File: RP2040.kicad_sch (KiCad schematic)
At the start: 30 parts, among them J1 USB_B_Micro, J2 Conn_01x03, SW1 SW_Push, SW2 SW_Push, U1 AMS1117-3.3, U5 W25Q128JVS, U6 RP2040, Y1 X322512MSB4SI

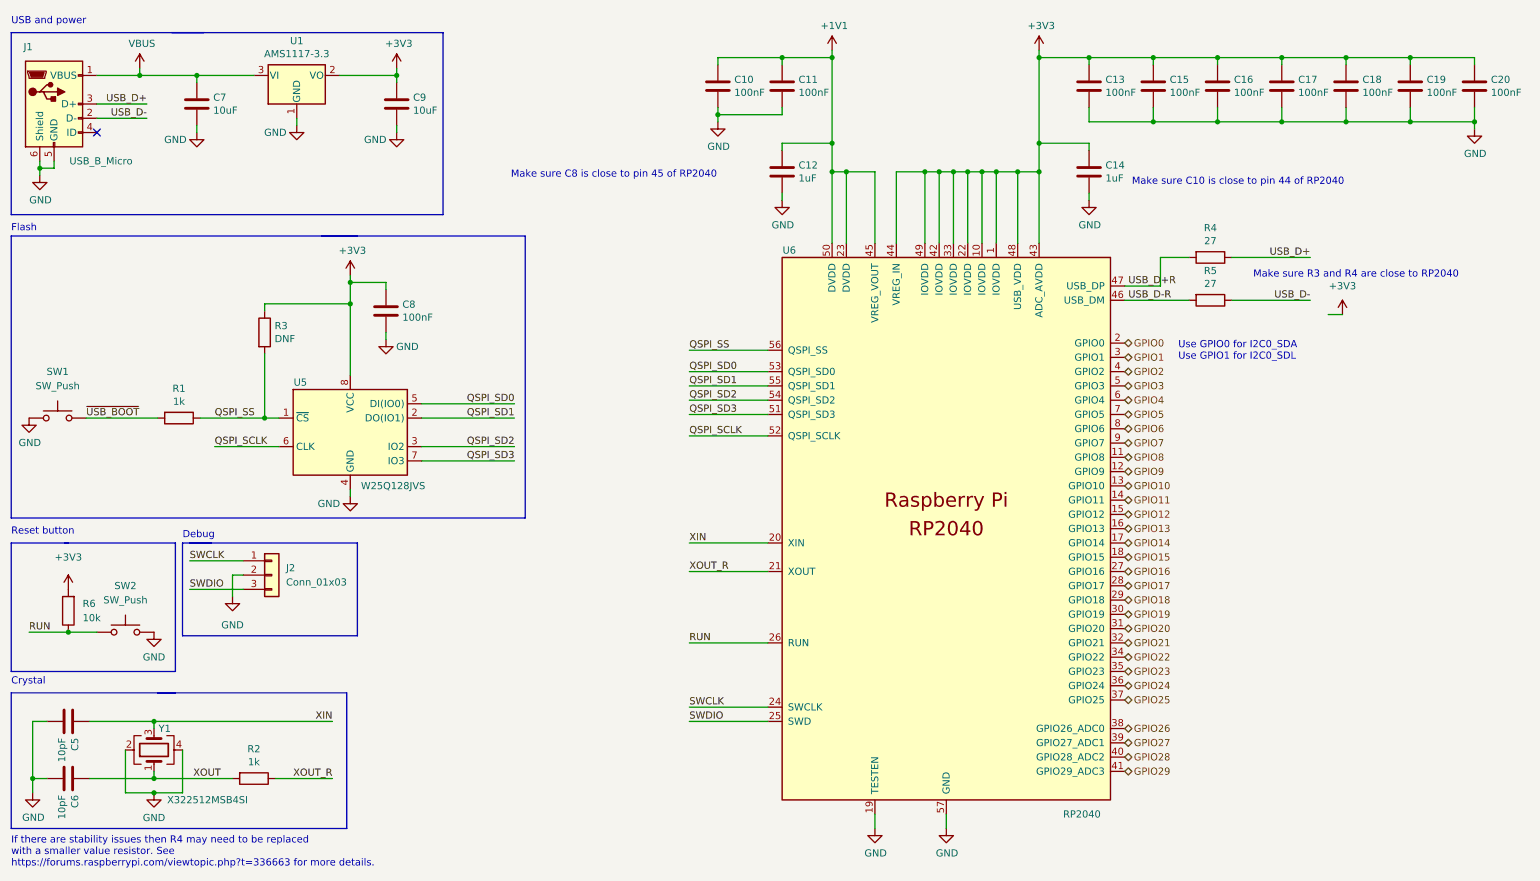
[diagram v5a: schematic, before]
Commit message: Redo RP2040 layout
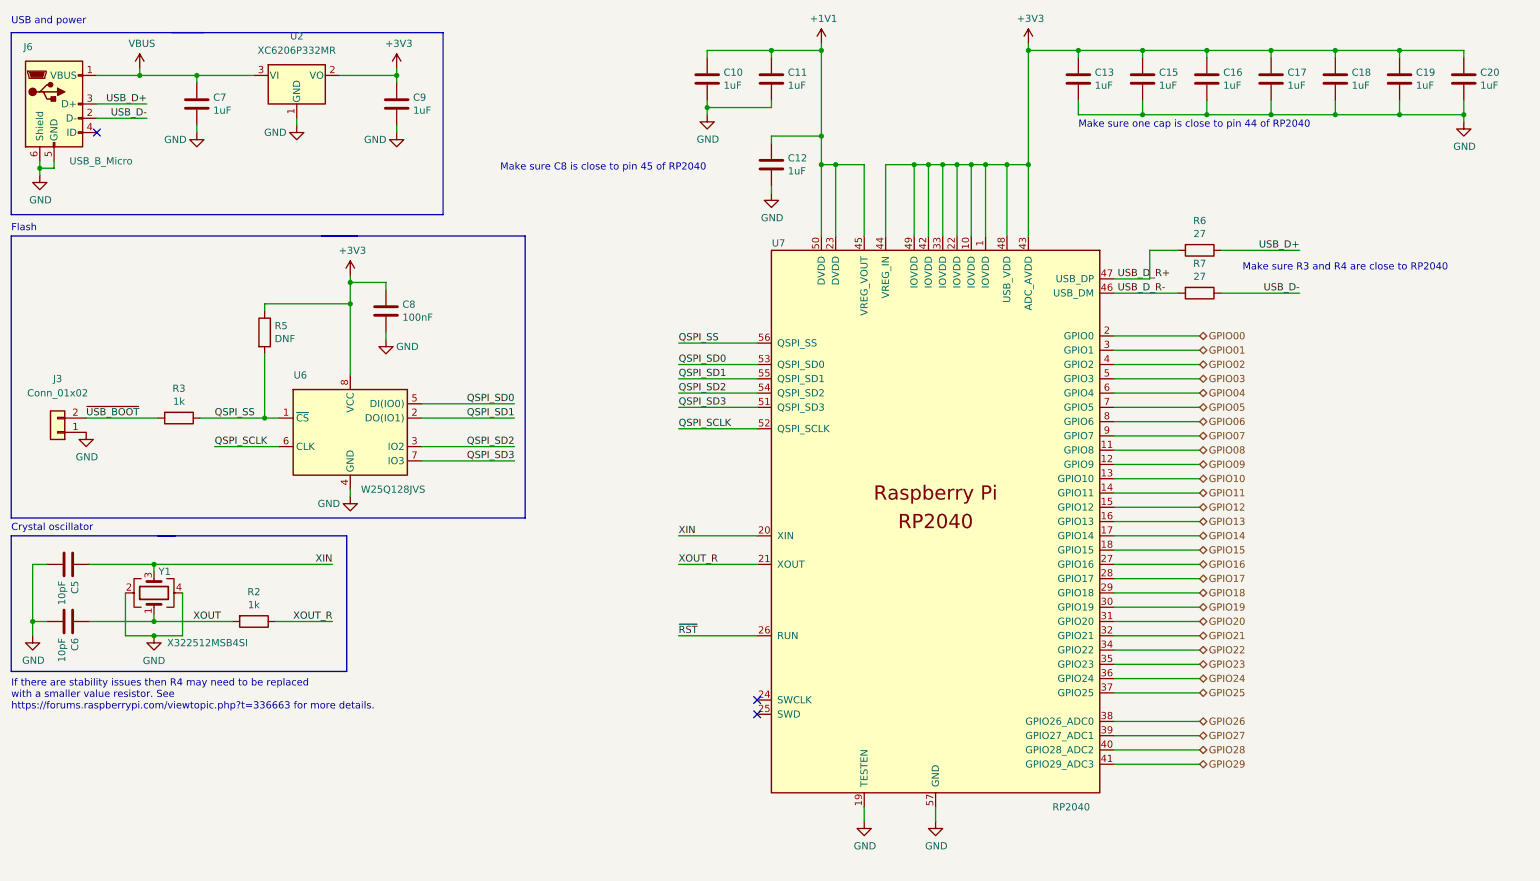
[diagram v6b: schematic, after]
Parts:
- removed C14: 1uF, Custom_Footprints:Perfect_0402, symbol Device:C
- removed J1: USB_B_Micro, Custom_Footprints:USB_B_Mini_Amphenol_UE25BE5510H, symbol Connector:USB_B_Micro
- removed J2: Conn_01x03, Connector_PinHeader_2.54mm:PinHeader_1x03_P2.54mm_Vertical, symbol Connector_Generic:Conn_01x03
- removed R1: 1k, Custom_Footprints:Perfect_0402, symbol Device:R
- removed R4: 27, Resistor_SMD:R_0603_1608Metric, symbol Device:R
- removed SW1, SW2: SW_Push, Button_Switch_SMD:SW_SPST_TL3342, symbol Switch:SW_Push
- removed U1: AMS1117-3.3, Package_TO_SOT_SMD:SOT-223-3_TabPin2, symbol Regulator_Linear:NCP1117-3.3_SOT223
- removed U5: W25Q128JVS, Package_SO:SOIC-8_5.23x5.23mm_P1.27mm, symbol Memory_Flash:W25Q128JVS
- removed U6: RP2040, Custom_Footprints:QFN-56-1EP_7x7mm_P0.4mm_EP3.2x3.2mm, symbol Custom_Symbols:RP2040
- added J3: Conn_01x02, Connector_PinHeader_2.54mm:PinHeader_1x02_P2.54mm_Vertical, symbol Connector_Generic:Conn_01x02
- added J6: USB_B_Micro, Custom_Footprints:USB_B_Mini_Amphenol_UE25BE5510H, symbol Connector:USB_B_Micro
- added R7: 27, Resistor_SMD:R_0603_1608Metric, symbol Device:R
- added U2: XC6206P332MR, Package_TO_SOT_SMD:SOT-23, symbol Regulator_Linear:XC6206PxxxMR
- added U6: W25Q128JVS, Package_SO:SOIC-8_5.23x5.23mm_P1.27mm, symbol Memory_Flash:W25Q128JVS
- added U7: RP2040, Custom_Footprints:QFN57P40_700X700X90L40X18T310N, symbol Custom_Symbols:RP2040
- C10, C11, C13, C15, C16, C17, C18, C19, C20: value 100nF -> 1uF; LCSC C1525 -> (none)
- C12: LCSC C52923 -> (none)
- C7, C9: value 10uF -> 1uF
- R3: value DNF -> 1k; footprint Resistor_SMD:R_1206_3216Metric_Pad1.30x1.75mm_HandSolder -> Custom_Footprints:Perfect_0402; JLC (none) -> 0402; LCSC (none) -> C11702
- R5: value 27 -> DNF; footprint Resistor_SMD:R_0603_1608Metric -> Resistor_SMD:R_1206_3216Metric_Pad1.30x1.75mm_HandSolder; JLC 0603 -> (none); LCSC C25190 -> (none)
- R6: value 10k -> 27; footprint Custom_Footprints:Perfect_0402 -> Resistor_SMD:R_0603_1608Metric; JLC (none) -> 0603; LCSC (none) -> C25190
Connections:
- net RUN is gone; now on net USB_D+: R6.1
- net USB_D-R is gone; now on net QSPI_SS: R5.2
- net +1V1: now also U7.23 (DVDD), U7.45 (VREG_VOUT), U7.50 (DVDD)
- net +3V3: now also R5.1, U2.2 (VO), U6.8 (VCC), U7.1 (IOVDD), U7.10 (IOVDD), U7.22 (IOVDD), U7.33 (IOVDD), U7.42 (IOVDD), U7.43 (ADC_AVDD), U7.44 (VREG_IN), U7.48 (USB_VDD), U7.49 (IOVDD); no longer R3.1, R6.2
- net GND: now also J3.1 (Pin_1), J6.5 (GND), J6.6 (Shield), U2.1 (GND), U6.4 (GND), U7.19 (TESTEN), U7.57 (GND)
- net GPIO10: now also U7.13 (GPIO10)
- net GPIO11: now also U7.14 (GPIO11)
- net GPIO12: now also U7.15 (GPIO12)
- net GPIO13: now also U7.16 (GPIO13)
- net GPIO14: now also U7.17 (GPIO14)
- net GPIO15: now also U7.18 (GPIO15)
- net GPIO16: now also U7.27 (GPIO16)
- net GPIO17: now also U7.28 (GPIO17)
- net GPIO18: now also U7.29 (GPIO18)
- net GPIO19: now also U7.30 (GPIO19)
- net GPIO20: now also U7.31 (GPIO20)
- net GPIO21: now also U7.32 (GPIO21)
- net GPIO22: now also U7.34 (GPIO22)
- net GPIO23: now also U7.35 (GPIO23)
- net GPIO24: now also U7.36 (GPIO24)
- net GPIO25: now also U7.37 (GPIO25)
- net GPIO26: now also U7.38 (GPIO26_ADC0)
- net GPIO27: now also U7.39 (GPIO27_ADC1)
- net GPIO28: now also U7.40 (GPIO28_ADC2)
- net GPIO29: now also U7.41 (GPIO29_ADC3)
- net QSPI_SCLK: now also U6.6 (CLK), U7.52 (QSPI_SCLK)
- net QSPI_SD0: now also U6.5 (DI(IO0)), U7.53 (QSPI_SD0)
- net QSPI_SD1: now also U6.2 (DO(IO1)), U7.55 (QSPI_SD1)
- net QSPI_SD2: now also U6.3 (IO2), U7.54 (QSPI_SD2)
- net QSPI_SD3: now also U6.7 (IO3), U7.51 (QSPI_SD3)
- net QSPI_SS: now also R3.1, U6.1 (~{CS}), U7.56 (QSPI_SS); no longer R3.2
- net USB_D+: now also J6.3 (D+)
- net USB_D-: now also J6.2 (D-), R7.1; no longer R5.1
- net VBUS: now also J6.1 (VBUS), U2.3 (VI)
- net XIN: now also U7.20 (XIN)
- net XOUT_R: now also U7.21 (XOUT)
- net ~{USB_BOOT}: now also R3.2, J3.2 (Pin_2)
- new net GPIO00: U7.2 (GPIO0)
- new net GPIO01: U7.3 (GPIO1)
- new net GPIO02: U7.4 (GPIO2)
- new net GPIO03: U7.5 (GPIO3)
- new net GPIO04: U7.6 (GPIO4)
- new net GPIO05: U7.7 (GPIO5)
- new net GPIO06: U7.8 (GPIO6)
- new net GPIO07: U7.9 (GPIO7)
- new net GPIO08: U7.11 (GPIO8)
- new net GPIO09: U7.12 (GPIO9)
- new net USB_D_R+: R6.2, U7.47 (USB_DP)
- new net USB_D_R-: R7.2, U7.46 (USB_DM)
- new net ~{RST}: U7.26 (RUN)
- no-connect marks 1 -> 3
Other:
- note added: "Crystal oscillator"
- note added: "Make sure one cap is close to pin 44 of RP2040"
- note removed: "Crystal"
- note removed: "Debug"
- note removed: "Make sure C10 is close to pin 44 of RP2040"
- note removed: "Reset button"
- note removed: "Use GPIO0 for I2C0_SDA Use GPIO1 for I2C0_SDL"
- moved on the sheet: C5, C6, R2, Y1

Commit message: Update external button connector, 3d models
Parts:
- U7: footprint Custom_Footprints:QFN57P40_700X700X90L40X18T310N -> Custom_Footprints:QFN56P40_700X700X90L40X18T310N
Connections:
- net VBUS renamed +5V
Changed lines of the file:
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@@
     (property "Reference" "U7" (id 0) (at 151.13 54.61 0))
     (property "Value" "RP2040" (id 1) (at 203.2 154.94 0))
-    (property "Footprint" "Custom_Footprints:QFN57P40_700X700X90L40X18T310N" (id 2) (at 179.07 168.275 0)
+    (property "Footprint" "Custom_Footprints:QFN56P40_700X700X90L40X18T310N" (id 2) (at 179.07 168.275 0)
       (effects (font (size 1.27 1.27)) hide)
     )
@@
     (pin "1")
   )
+  (symbol (lib_id "power:+5V") (at 37.465 23.495 0) (unit 1)
+    (in_bom yes) (on_board yes)
+    (property "Reference" "#PWR0113" (id 0) (at 37.465 27.305 0)
+      (effects (font (size 1.27 1.27)) hide)
+    )
+    (property "Value" "+5V" (id 1) (at 37.465 19.685 0))
+    (property "Footprint" "" (id 2) (at 37.465 23.495 0)
+      (effects (font (size 1.27 1.27)) hide)
+    )
+    (property "Datasheet" "" (id 3) (at 37.465 23.495 0)
+      (effects (font (size 1.27 1.27)) hide)
+    )
+    (pin "1")
+  )
   (symbol (lib_id "power:+3V3") (at 83.185 23.495 0) (unit 1)
     (in_bom yes) (on_board yes)
@@
     (pin "8")
   )
-  (symbol (lib_id "power:VBUS") (at 37.465 23.495 0) (unit 1)
-    (in_bom yes) (on_board yes)
-    (property "Reference" "#PWR0107" (id 0) (at 37.465 27.305 0)
-      (effects (font (size 1.27 1.27)) hide)
-    )
-    (property "Value" "VBUS" (id 1) (at 37.846 19.1008 0))
-    (property "Footprint" "" (id 2) (at 37.465 23.495 0)
-      (effects (font (size 1.27 1.27)) hide)
-    )
-    (property "Datasheet" "" (id 3) (at 37.465 23.495 0)
-      (effects (font (size 1.27 1.27)) hide)
-    )
-    (pin "1")
-  )
   (symbol (lib_id "Device:C") (at 47.625 29.845 0) (unit 1)
